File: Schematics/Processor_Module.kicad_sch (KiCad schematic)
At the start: 8 parts, among them J1 Conn_01x02, J2 To Compute #1, J3 Conn_01x04, J4 Conn_01x04, J5 To Compute #1, U1 USB Host Shield 2.0, U2 ESP32-DEVKIT-V1

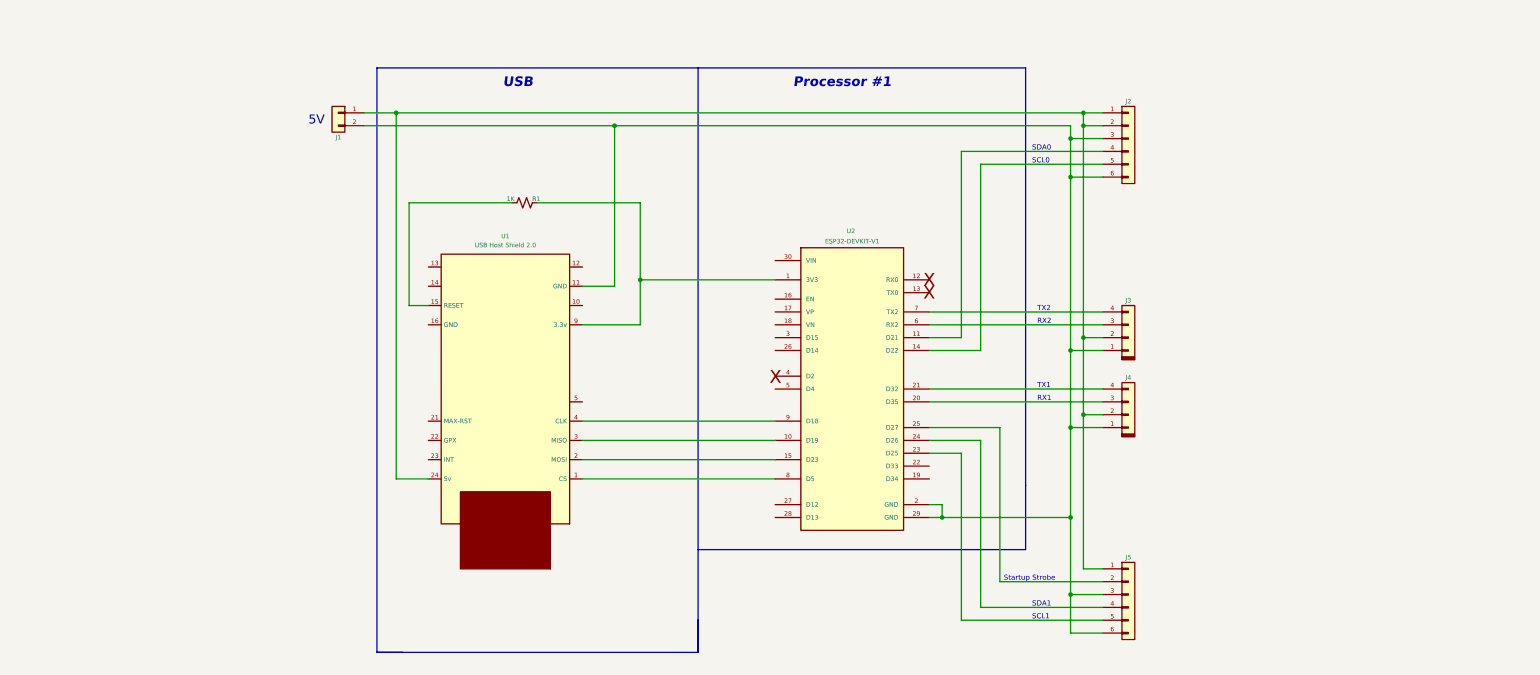
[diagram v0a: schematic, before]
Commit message: All Oscillators have thier own D/A converters and both LFOs are working.  Callibration functions.
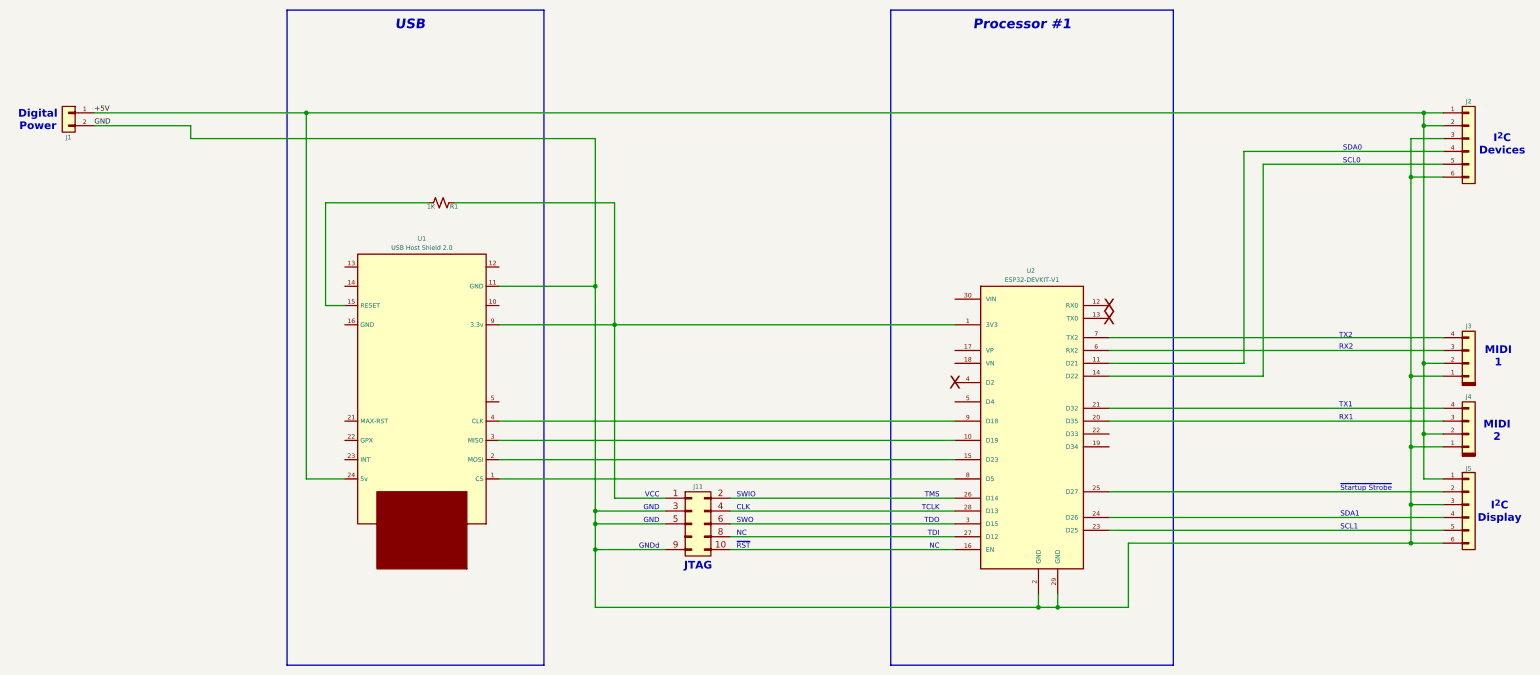
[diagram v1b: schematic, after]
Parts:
- added J11: Conn_02x05_Odd_Even, symbol Connector_keyed_kicad_sym:Conn_02x05_Odd_Even
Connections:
- net at R1.1, U1.9 (3.3v), U2.1 (3V3): now also J11.1 (Pin_1)
- net at U2.16 (EN): now also J11.10 (Pin_10)
- net GND: now reaches J1.2 (Pin_2), J2.3 (Pin_3), J2.6 (Pin_6), J3.1 (Pin_1), J4.1 (Pin_1), J5.3 (Pin_3), J5.6 (Pin_6), U1.11 (GND), U2.2 (GND), U2.29 (GND)
- net GND: now also J11.3 (Pin_3), J11.5 (Pin_5), J11.9 (Pin_9)
- net at U2.26 (D14): now also J11.2 (Pin_2)
- net at U2.27 (D12): now also J11.8 (Pin_8)
- net at U2.28 (D13): now also J11.4 (Pin_4)
- net at U2.3 (D15): now also J11.6 (Pin_6)
- net +5V: now reaches J1.1 (Pin_1), J2.1 (Pin_1), J2.2 (Pin_2), J3.2 (Pin_2), J4.2 (Pin_2), J5.1 (Pin_1), U1.24 (5v)
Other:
- note added: "CLK"
- note added: "Digital Power"
- note added: "GND"
- note added: "GNDd"
- note added: "I^{2}C Devices"
- note added: "I^{2}C Display"
- note added: "JTAG"
- note added: "MIDI 1"
- note added: "MIDI 2"
- note added: "NC"
- note added: "SWIO"
- note added: "SWO"
- note added: "TCLK"
- note added: "TDI"
- note added: "TDO"
- note added: "TMS"
- note added: "VCC"
- note added: "~{RST}"
- note added: "~{Startup Strobe}"
- note removed: "5V"
- note removed: "Startup Strobe"
- moved on the sheet: J1, J2, J3, J4, J5, R1, U1, U2

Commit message: Fixed bugs in voice selection on configuration.  Reorganized schematics to have different master drawings for power and audio paths.  Started work on dual 3-pole state variable filter with resonance.
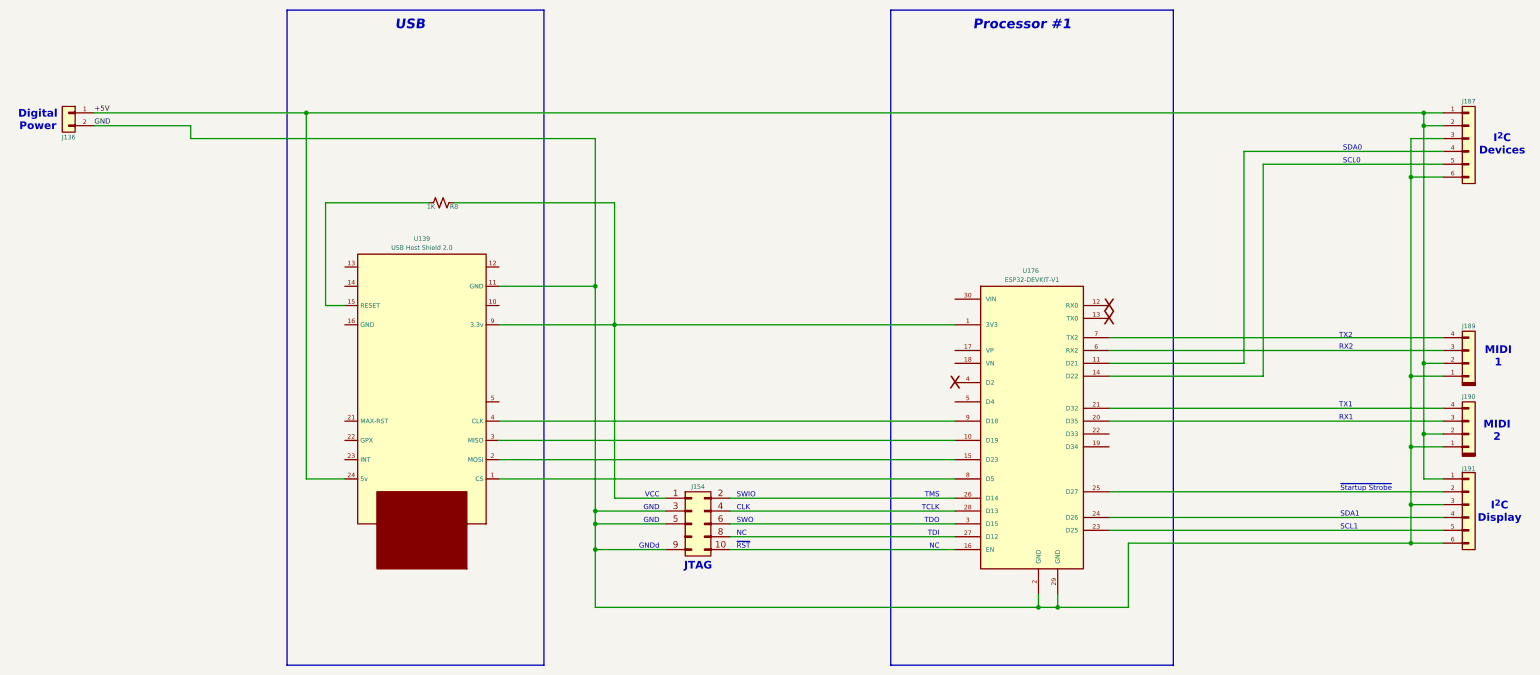
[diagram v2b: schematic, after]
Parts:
- renumbered J1 to J136, J11 to J154, J2 to J187, J3 to J189, J4 to J190, J5 to J191, R1 to R8, U1 to U139, U2 to U176
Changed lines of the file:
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@@
 		(on_board yes)
 		(dnp no)
-		(property "Reference" "U2"
+		(property "Reference" "U176"
 			(at 224.536 76.962 0)
 			(effects
@@
 		(instances
 			(project "Synth32"
-				(path "/718f017d-28fe-4e29-b548-40db8e21cec7/5f23d779-3412-4b06-96f4-480c60744fb9"
-					(reference "U2")
+				(path "/718f017d-28fe-4e29-b548-40db8e21cec7/33a531ad-adab-44e4-8605-e758909b7125/aad42c90-a42a-4d30-bdda-262c4c717c2c"
+					(reference "U176")
 					(unit 1)
 				)
@@
 		(on_board yes)
 		(dnp no)
-		(property "Reference" "J2"
+		(property "Reference" "J187"
 			(at 311.15 43.434 0)
 			(effects
@@
 		(instances
 			(project "Synth32"
-				(path "/718f017d-28fe-4e29-b548-40db8e21cec7/5f23d779-3412-4b06-96f4-480c60744fb9"
-					(reference "J2")
+				(path "/718f017d-28fe-4e29-b548-40db8e21cec7/33a531ad-adab-44e4-8605-e758909b7125/aad42c90-a42a-4d30-bdda-262c4c717c2c"
+					(reference "J187")
 					(unit 1)
 				)
@@
 		(on_board yes)
 		(dnp no)
-		(property "Reference" "J1"
+		(property "Reference" "J136"
 			(at 34.29 50.546 0)
 			(effects
@@
 		(instances
 			(project "Synth32"
-				(path "/718f017d-28fe-4e29-b548-40db8e21cec7/5f23d779-3412-4b06-96f4-480c60744fb9"
-					(reference "J1")
+				(path "/718f017d-28fe-4e29-b548-40db8e21cec7/33a531ad-adab-44e4-8605-e758909b7125/aad42c90-a42a-4d30-bdda-262c4c717c2c"
+					(reference "J136")
 					(unit 1)
 				)
@@
 		(on_board yes)
 		(dnp no)
-		(property "Reference" "J11"
+		(property "Reference" "J154"
 			(at 158.75 119.634 0)
 			(effects
@@
 		(instances
 			(project "Synth32"
-				(path "/718f017d-28fe-4e29-b548-40db8e21cec7/5f23d779-3412-4b06-96f4-480c60744fb9"
-					(reference "J11")
+				(path "/718f017d-28fe-4e29-b548-40db8e21cec7/33a531ad-adab-44e4-8605-e758909b7125/aad42c90-a42a-4d30-bdda-262c4c717c2c"
+					(reference "J154")
 					(unit 1)
 				)
@@
 		(on_board yes)
 		(dnp no)
-		(property "Reference" "J5"
+		(property "Reference" "J191"
 			(at 311.15 116.078 0)
 			(effects
@@
 		(instances
 			(project "Synth32"
-				(path "/718f017d-28fe-4e29-b548-40db8e21cec7/5f23d779-3412-4b06-96f4-480c60744fb9"
-					(reference "J5")
+				(path "/718f017d-28fe-4e29-b548-40db8e21cec7/33a531ad-adab-44e4-8605-e758909b7125/aad42c90-a42a-4d30-bdda-262c4c717c2c"
+					(reference "J191")
 					(unit 1)
 				)
@@
 		(on_board yes)
 		(dnp no)
-		(property "Reference" "J4"
+		(property "Reference" "J190"
 			(at 311.15 101.854 0)
 			(effects
@@
 		(instances
 			(project "Synth32"
-				(path "/718f017d-28fe-4e29-b548-40db8e21cec7/5f23d779-3412-4b06-96f4-480c60744fb9"
-					(reference "J4")
+				(path "/718f017d-28fe-4e29-b548-40db8e21cec7/33a531ad-adab-44e4-8605-e758909b7125/aad42c90-a42a-4d30-bdda-262c4c717c2c"
+					(reference "J190")
 					(unit 1)
 				)
@@
 		(on_board yes)
 		(dnp no)
-		(property "Reference" "U1"
+		(property "Reference" "U139"
 			(at 104.14 70.612 0)
 			(effects
@@
 		(instances
 			(project "Synth32"
-				(path "/718f017d-28fe-4e29-b548-40db8e21cec7/5f23d779-3412-4b06-96f4-480c60744fb9"
-					(reference "U1")
+				(path "/718f017d-28fe-4e29-b548-40db8e21cec7/33a531ad-adab-44e4-8605-e758909b7125/aad42c90-a42a-4d30-bdda-262c4c717c2c"
+					(reference "U139")
 					(unit 1)
 				)
@@
 		(on_board yes)
 		(dnp no)
-		(property "Reference" "R1"
+		(property "Reference" "R8"
 			(at 110.49 64.262 90)
 			(effects
@@
 		(instances
 			(project "Synth32"
-				(path "/718f017d-28fe-4e29-b548-40db8e21cec7/5f23d779-3412-4b06-96f4-480c60744fb9"
-					(reference "R1")
+				(path "/718f017d-28fe-4e29-b548-40db8e21cec7/33a531ad-adab-44e4-8605-e758909b7125/aad42c90-a42a-4d30-bdda-262c4c717c2c"
+					(reference "R8")
 					(unit 1)
 				)
@@
 		(on_board yes)
 		(dnp no)
-		(property "Reference" "J3"
+		(property "Reference" "J189"
 			(at 311.15 87.884 0)
 			(effects
@@
 		(instances
 			(project "Synth32"
-				(path "/718f017d-28fe-4e29-b548-40db8e21cec7/5f23d779-3412-4b06-96f4-480c60744fb9"
-					(reference "J3")
-					(unit 1)
-				)
+				(path "/718f017d-28fe-4e29-b548-40db8e21cec7/33a531ad-adab-44e4-8605-e758909b7125/aad42c90-a42a-4d30-bdda-262c4c717c2c"
+					(reference "J189")
+					(unit 1)
+				)
